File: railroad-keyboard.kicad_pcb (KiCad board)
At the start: 2 copper layers, 208 parts, among them SW1 SW_Push, U1 ATmega32U4-AU, Y1 16MHz

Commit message: Further PCB WIP
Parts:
- moved MX609 403.5 mm to (388.1, 304.8)
- moved MX509 403.0 mm to (407.2, 285.8)
- moved MX810 390.5 mm to (438.1, 328.6)
- moved MX909 377.9 mm to (419.1, 328.6)
- moved MX908 370.8 mm to (371.5, 323.9)
- moved MX809 365.2 mm to (400.1, 328.6)
- moved MX808 345.6 mm to (342.9, 323.9)
- moved MX906 326.7 mm to (288.1, 328.6)
- moved MX708 323.1 mm to (361.9, 304.8)
- moved MX907 314.9 mm to (314.3, 328.6)
- moved MX608 311.5 mm to (342.9, 304.8)
- moved MX600 303.1 mm to (9.53, 309.6)
- moved MX904 300.7 mm to (202.4, 328.6)
- moved MX707 298.6 mm to (323.9, 304.8)
- moved MX702 285.7 mm to (123.8, 304.8)
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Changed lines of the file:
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@@
   )
   (module MX_Alps_Hybrid:MX-1U-NoLED (layer F.Cu)
-    (at 195.78 23.78875)
+    (at 419.1 328.6125)
     (fp_text reference MX909 (at 0 3.175) (layer Dwgs.User)
       (effects (font (size 1 1) (thickness 0.15)))
@@
   )
   (module MX_Alps_Hybrid:MX-1.5U-NoLED (layer F.Cu)
-    (at 57.8425 126.06875)
+    (at 371.475 323.85)
     (fp_text reference MX908 (at 0 3.175) (layer Dwgs.User)
       (effects (font (size 1 1) (thickness 0.15)))
@@
   )
   (module MX_Alps_Hybrid:MX-1U-NoLED (layer F.Cu)
-    (at 43.56 167.74875)
+    (at 314.325 328.6125)
     (fp_text reference MX907 (at 0 3.175) (layer Dwgs.User)
       (effects (font (size 1 1) (thickness 0.15)))
@@
   )
   (module MX_Alps_Hybrid:MX-1.75U-NoLED (layer F.Cu)
-    (at 69.75375 85.66875)
+    (at 288.13125 328.6125)
     (fp_text reference MX906 (at 0 3.175) (layer Dwgs.User)
       (effects (font (size 1 1) (thickness 0.15)))
@@
   )
   (module MX_Alps_Hybrid:MX-2.25U-NoLED (layer F.Cu)
-    (at 504.825 284.95625)
+    (at 250.03125 328.6125)
     (fp_text reference MX905 (at 0 3.175) (layer Dwgs.User)
       (effects (font (size 1 1) (thickness 0.15)))
@@
   )
   (module MX_Alps_Hybrid:MX-2.75U-NoLED (layer F.Cu)
-    (at 494.50625 257.175)
+    (at 202.40625 328.6125)
     (fp_text reference MX904 (at 0 3.175) (layer Dwgs.User)
       (effects (font (size 1 1) (thickness 0.15)))
@@
   )
   (module MX_Alps_Hybrid:MX-1.75U-NoLED (layer F.Cu)
-    (at 25.74375 107.14875)
+    (at 159.54375 328.6125)
     (fp_text reference MX903 (at 0 3.175) (layer Dwgs.User)
       (effects (font (size 1 1) (thickness 0.15)))
@@
   )
   (module MX_Alps_Hybrid:MX-1U-NoLED (layer F.Cu)
-    (at 53.08 146.26875)
+    (at 133.35 328.6125)
     (fp_text reference MX902 (at 0 3.175) (layer Dwgs.User)
       (effects (font (size 1 1) (thickness 0.15)))
@@
   )
   (module MX_Alps_Hybrid:MX-1.25U-NoLED (layer F.Cu)
-    (at 89.95125 105.86875)
+    (at 83.34375 323.85)
     (fp_text reference MX901 (at 0 3.175) (layer Dwgs.User)
       (effects (font (size 1 1) (thickness 0.15)))
@@
   )
   (module MX_Alps_Hybrid:MX-1U-NoLED (layer F.Cu)
-    (at 82.8 126.06875)
+    (at 28.575 328.6125)
     (fp_text reference MX900 (at 0 3.175) (layer Dwgs.User)
       (effects (font (size 1 1) (thickness 0.15)))
@@
   )
   (module MX_Alps_Hybrid:MX-1U-NoLED (layer F.Cu)
-    (at 170.82 43.98875)
+    (at 438.15 328.6125)
     (fp_text reference MX810 (at 0 3.175) (layer Dwgs.User)
       (effects (font (size 1 1) (thickness 0.15)))
@@
   )
   (module MX_Alps_Hybrid:MX-1U-NoLED (layer F.Cu)
-    (at 112.53 103.43875)
+    (at 400.05 328.6125)
     (fp_text reference MX809 (at 0 3.175) (layer Dwgs.User)
       (effects (font (size 1 1) (thickness 0.15)))
@@
   )
   (module MX_Alps_Hybrid:MX-1.5U-NoLED (layer F.Cu)
-    (at 116.1425 63.03875)
+    (at 342.9 323.85)
     (fp_text reference MX808 (at 0 3.175) (layer Dwgs.User)
       (effects (font (size 1 1) (thickness 0.15)))
@@
   )
   (module MX_Alps_Hybrid:MX-1.25U-NoLED (layer F.Cu)
-    (at 20.98125 167.74875)
+    (at 107.15625 323.85)
     (fp_text reference MX802 (at 0 3.175) (layer Dwgs.User)
       (effects (font (size 1 1) (thickness 0.15)))
@@
   )
   (module MX_Alps_Hybrid:MX-1.5U-NoLED (layer F.Cu)
-    (at 62.6125 105.86875)
+    (at 57.15 323.85)
     (fp_text reference MX801 (at 0 3.175) (layer Dwgs.User)
       (effects (font (size 1 1) (thickness 0.15)))
@@
   )
   (module MX_Alps_Hybrid:MX-1U-NoLED (layer F.Cu)
-    (at 73.28 146.26875)
+    (at 9.525 328.6125)
     (fp_text reference MX800 (at 0 3.175) (layer Dwgs.User)
       (effects (font (size 1 1) (thickness 0.15)))
@@
   )
   (module MX_Alps_Hybrid:MX-1U-NoLED (layer F.Cu)
-    (at 224.2 124.78875)
+    (at 419.1 309.5625)
     (fp_text reference MX709 (at 0 3.175) (layer Dwgs.User)
       (effects (font (size 1 1) (thickness 0.15)))
@@
   )
   (module MX_Alps_Hybrid:MX-1U-NoLED (layer F.Cu)
-    (at 126.81 83.23875)
+    (at 361.95 304.8)
     (fp_text reference MX708 (at 0 3.175) (layer Dwgs.User)
       (effects (font (size 1 1) (thickness 0.15)))
@@
   )
   (module MX_Alps_Hybrid:MX-1U-NoLED (layer F.Cu)
-    (at 147.01 64.18875)
+    (at 323.85 304.8)
     (fp_text reference MX707 (at 0 3.175) (layer Dwgs.User)
       (effects (font (size 1 1) (thickness 0.15)))
@@
   )
   (module MX_Alps_Hybrid:MX-1U-NoLED (layer F.Cu)
-    (at 211.22 43.98875)
+    (at 285.75 304.8)
     (fp_text reference MX706 (at 0 3.175) (layer Dwgs.User)
       (effects (font (size 1 1) (thickness 0.15)))
@@
   )
   (module MX_Alps_Hybrid:MX-1U-NoLED (layer F.Cu)
-    (at 256.38 23.78875)
+    (at 242.8875 304.8)
     (fp_text reference MX705 (at 0 3.175) (layer Dwgs.User)
       (effects (font (size 1 1) (thickness 0.15)))
@@
   )
   (module MX_Alps_Hybrid:MX-1U-NoLED (layer F.Cu)
-    (at 133.88 144.98875)
+    (at 204.7875 304.8)
     (fp_text reference MX704 (at 0 3.175) (layer Dwgs.User)
       (effects (font (size 1 1) (thickness 0.15)))
@@
   )
   (module MX_Alps_Hybrid:MX-1U-NoLED (layer F.Cu)
-    (at 231.42 43.98875)
+    (at 161.925 304.8)
     (fp_text reference MX703 (at 0 3.175) (layer Dwgs.User)
       (effects (font (size 1 1) (thickness 0.15)))
@@
   )
   (module MX_Alps_Hybrid:MX-1U-NoLED (layer F.Cu)
-    (at 175.58 23.78875)
+    (at 123.825 304.8)
     (fp_text reference MX702 (at 0 3.175) (layer Dwgs.User)
       (effects (font (size 1 1) (thickness 0.15)))
@@
   )
   (module MX_Alps_Hybrid:MX-1U-NoLED (layer F.Cu)
-    (at 147.01 84.38875)
+    (at 85.725 304.8)
     (fp_text reference MX701 (at 0 3.175) (layer Dwgs.User)
       (effects (font (size 1 1) (thickness 0.15)))
@@
   )
   (module MX_Alps_Hybrid:MX-1.75U-NoLED (layer F.Cu)
-    (at 25.74375 127.34875)
+    (at 388.14375 304.8)
     (fp_text reference MX609 (at 0 3.175) (layer Dwgs.User)
       (effects (font (size 1 1) (thickness 0.15)))
@@
   )
   (module MX_Alps_Hybrid:MX-1U-NoLED (layer F.Cu)
-    (at 63.76 166.46875)
+    (at 342.9 304.8)
     (fp_text reference MX608 (at 0 3.175) (layer Dwgs.User)
       (effects (font (size 1 1) (thickness 0.15)))
@@
   )
   (module MX_Alps_Hybrid:MX-1U-NoLED (layer F.Cu)
-    (at 191.02 43.98875)
+    (at 304.8 304.8)
     (fp_text reference MX607 (at 0 3.175) (layer Dwgs.User)
       (effects (font (size 1 1) (thickness 0.15)))
@@
   )
   (module MX_Alps_Hybrid:MX-1U-NoLED (layer F.Cu)
-    (at 93.48 146.26875)
+    (at 266.7 304.8)
     (fp_text reference MX606 (at 0 3.175) (layer Dwgs.User)
       (effects (font (size 1 1) (thickness 0.15)))
@@
   )
   (module MX_Alps_Hybrid:MX-1U-NoLED (layer F.Cu)
-    (at 215.98 23.78875)
+    (at 223.8375 304.8)
     (fp_text reference MX605 (at 0 3.175) (layer Dwgs.User)
       (effects (font (size 1 1) (thickness 0.15)))
@@
   )
   (module MX_Alps_Hybrid:MX-1U-NoLED (layer F.Cu)
-    (at 187.41 84.38875)
+    (at 180.975 304.8)
     (fp_text reference MX604 (at 0 3.175) (layer Dwgs.User)
       (effects (font (size 1 1) (thickness 0.15)))
@@
   )
   (module MX_Alps_Hybrid:MX-1U-NoLED (layer F.Cu)
-    (at 167.21 84.38875)
+    (at 142.875 304.8)
     (fp_text reference MX603 (at 0 3.175) (layer Dwgs.User)
       (effects (font (size 1 1) (thickness 0.15)))
@@
   )
   (module MX_Alps_Hybrid:MX-1U-NoLED (layer F.Cu)
-    (at 83.96 166.46875)
+    (at 104.775 304.8)
     (fp_text reference MX602 (at 0 3.175) (layer Dwgs.User)
       (effects (font (size 1 1) (thickness 0.15)))
@@
   )
   (module MX_Alps_Hybrid:MX-2.75U-NoLED (layer F.Cu)
-    (at 35.26875 44.62875)
+    (at 50.00625 304.8)
     (fp_text reference MX601 (at 0 3.175) (layer Dwgs.User)
       (effects (font (size 1 1) (thickness 0.15)))
@@
   )
   (module MX_Alps_Hybrid:MX-1U-NoLED (layer F.Cu)
-    (at 187.41 64.18875)
+    (at 9.525 309.5625)
     (fp_text reference MX600 (at 0 3.175) (layer Dwgs.User)
       (effects (font (size 1 1) (thickness 0.15)))
@@
   )
   (module MX_Alps_Hybrid:MX-1.75U-NoLED (layer F.Cu)
-    (at 69.75375 65.46875)
+    (at 407.19375 285.75)
     (fp_text reference MX509 (at 0 3.175) (layer Dwgs.User)
       (effects (font (size 1 1) (thickness 0.15)))
@@
   )
   (module MX_Alps_Hybrid:MX-1U-NoLED (layer F.Cu)
-    (at 143.4 104.58875)
+    (at 361.95 285.75)
     (fp_text reference MX508 (at 0 3.175) (layer Dwgs.User)
       (effects (font (size 1 1) (thickness 0.15)))
@@
   )
   (module MX_Alps_Hybrid:MX-1U-NoLED (layer F.Cu)
-    (at 167.21 64.18875)
+    (at 323.85 285.75)
     (fp_text reference MX507 (at 0 3.175) (layer Dwgs.User)
       (effects (font (size 1 1) (thickness 0.15)))
@@
   )
   (module MX_Alps_Hybrid:MX-1U-NoLED (layer F.Cu)
-    (at 207.61 84.38875)
+    (at 381 285.75)
     (fp_text reference MX409 (at 0 3.175) (layer Dwgs.User)
       (effects (font (size 1 1) (thickness 0.15)))
@@
   )
   (module MX_Alps_Hybrid:MX-1U-NoLED (layer F.Cu)
-    (at 227.81 64.18875)
+    (at 342.9 285.75)
     (fp_text reference MX408 (at 0 3.175) (layer Dwgs.User)
       (effects (font (size 1 1) (thickness 0.15)))
@@
   )
   (module MX_Alps_Hybrid:MX-1U-NoLED (layer F.Cu)
-    (at 251.62 43.98875)
+    (at 304.8 285.75)
     (fp_text reference MX407 (at 0 3.175) (layer Dwgs.User)
       (effects (font (size 1 1) (thickness 0.15)))

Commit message: Diodes placed
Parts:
- D0, D1, D10, D100, D101, D102, D103, D104, D105, D106, D107, D108, D109, D2, D200, D201, D202, D203, D204, D205, D206, D207, D208, D209, D3, D300, D301, D302, D303, D304, D305, D306, D307, D308, D309, D4, D400, D401, D402, D403, D404, D405, D406, D407, D408, D409, D410, D5, D501, D502, D503, D504, D505, D506, D507, D508, D509, D6, D600, D601, D602, D603, D604, D605, D606, D607, D608, D609, D7, D701, D702, D703, D704, D705, D706, D707, D708, D709, D8, D800, D801, D802, D808, D809, D810, D9, D900, D901, D902, D903, D904, D905, D906, D907, D908, D909: moved to B.Cu
- moved D810 435.1 mm to (446.4, 331.2), turned to 90 degrees
- moved D909 420.2 mm to (427.2, 331.1), turned to 90 degrees
- moved D709 408.7 mm to (427.2, 312.2), turned to 90 degrees
- moved D410 378.5 mm to (436.1, 284.5)
- moved D609 367.0 mm to (396.4, 307.3), turned to 90 degrees
- moved D509 364.4 mm to (415.4, 288.3), turned to 90 degrees
- moved D809 364.0 mm to (408.2, 331.1), turned to 90 degrees
- moved D708 349.9 mm to (370.1, 307.3), turned to 90 degrees
- moved D908 347.9 mm to (379.6, 326.4), turned to 90 degrees
- moved D10 345.0 mm to (446.3, 250.2), turned to 90 degrees
- moved D309 344.8 mm to (417.7, 269.2), turned to 90 degrees
- moved D109 332.5 mm to (427.2, 250.2), turned to 90 degrees
- moved D409 329.3 mm to (389.1, 288.3), turned to 90 degrees
- moved D907 328.0 mm to (322.5, 331.1), turned to 270 degrees
- moved D209 327.4 mm to (394.0, 269.2), turned to 90 degrees
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
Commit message: Completion of first draft
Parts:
- C1, C2, C3, C4, C5, C6, C7, F1, R1, R2, R3, R4, SW1, U1, USB1, Y1: moved to B.Cu
- MX0, MX1, MX10, MX101, MX102, MX103, MX104, MX105, MX106, MX107, MX108, MX109, MX2, MX200, MX202, MX203, MX204, MX205, MX206, MX207, MX208, MX3, MX301, MX302, MX303, MX304, MX305, MX306, MX307, MX308, MX309, MX4, MX402, MX403, MX404, MX405, MX406, MX407, MX408, MX409, MX5, MX501, MX502, MX503, MX504, MX505, MX506, MX507, MX6, MX600, MX602, MX603, MX604, MX605, MX606, MX607, MX608, MX7, MX701, MX702, MX703, MX704, MX705, MX706, MX707, MX708, MX709, MX8, MX800, MX809, MX810, MX900, MX902, MX907, MX909: footprint MX_Alps_Hybrid:MX-1U-NoLED -> MX_Only:MXOnly-1U-NoLED
- MX100, MX9: footprint MX_Alps_Hybrid:MX-2U-NoLED -> MX_Only:MXOnly-2U-NoLED
- MX201, MX209, MX300, MX801, MX808, MX908: footprint MX_Alps_Hybrid:MX-1.5U-NoLED -> MX_Only:MXOnly-1.5U-NoLED
- MX400, MX802, MX901: footprint MX_Alps_Hybrid:MX-1.25U-NoLED -> MX_Only:MXOnly-1.25U-NoLED
- MX401, MX905: footprint MX_Alps_Hybrid:MX-2.25U-NoLED -> MX_Only:MXOnly-2.25U-NoLED
- MX410: footprint MX_Alps_Hybrid:MX-ISO -> MX_Only:MXOnly-ISO-ROTATED-ReversedStabilizers-NoLED
- MX508: footprint MX_Alps_Hybrid:MX-1U-NoLED -> MX_Only:MXOnly-1.75U-NoLED
- MX509, MX609, MX903, MX906: footprint MX_Alps_Hybrid:MX-1.75U-NoLED -> MX_Only:MXOnly-1.75U-NoLED
- MX601, MX904: footprint MX_Alps_Hybrid:MX-2.75U-NoLED -> MX_Only:MXOnly-2.75U-NoLED
- moved R4 442.0 mm to (445.5, 315.9), turned to 90 degrees
- moved R1 441.6 mm to (434.2, 298.3), turned to 180 degrees
- moved U1 440.2 mm to (438.8, 306.7)
- moved R2 415.3 mm to (431.5, 250.8)
- moved R3 415.2 mm to (428.2, 248.9)
- moved C1 395.2 mm to (440.6, 292.7), turned to 90 degrees
- moved USB1 382.9 mm to (428.6, 241.8), turned to 270 degrees
- moved C6 341.0 mm to (441.1, 316.1), turned to 180 degrees
- moved C3 331.4 mm to (428.6, 306.6), turned to 270 degrees
- moved C5 327.3 mm to (430.0, 314.2), turned to 270 degrees
- moved C2 325.2 mm to (432.1, 291.3), turned to 90 degrees
- moved C7 314.8 mm to (440.3, 258.6), turned to 180 degrees
- moved Y1 314.1 mm to (436.4, 292.4), turned to 180 degrees
- moved C4 307.5 mm to (433.8, 258.6)
- moved F1 286.5 mm to (422.1, 241.3), turned to 90 degrees
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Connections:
- U1 pad 10: ROW2 -> COL2
- U1 pad 11: ROW3 -> COL3
- U1 pad 12: ROW7 -> COL4
- U1 pad 18: COL0 -> COL5
- U1 pad 19: COL1 -> COL6
- U1 pad 20: COL2 -> COL7
- U1 pad 21: COL3 -> COL8
- U1 pad 22: COL5 -> COL9
- U1 pad 25: COL4 -> COL10
- U1 pad 26: COL6 -> ROW0
- U1 pad 27: COL7 -> ROW1
- U1 pad 28: ROW4 -> ROW2
- U1 pad 29: ROW5 -> ROW3
- U1 pad 30: ROW6 -> ROW5
- U1 pad 31: ROW8 -> ROW4
- U1 pad 32: ROW9 -> ROW8
- U1 pad 39: COL10 -> ROW9
- U1 pad 40: COL9 -> ROW6
- U1 pad 41: COL8 -> ROW7
- U1 pad 8: ROW0 -> COL0
- U1 pad 9: ROW1 -> COL1
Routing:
- net COL0: track 0.00 -> 670.5 mm, vias 0 -> 2
- net COL1: track 0.00 -> 603.5 mm, vias 0 -> 2
- net GND: track 0.00 -> 570.5 mm, vias 0 -> 5
- net COL2: track 0.00 -> 527.9 mm, vias 0 -> 2
- net ROW0: track 0.00 -> 495.6 mm, vias 0 -> 2
- net Net-(R1-Pad2): track 0.00 -> 475.9 mm, vias 0 -> 2
- net ROW2: track 0.00 -> 475.2 mm, vias 0 -> 2
- net ROW8: track 0.00 -> 464.9 mm, vias 0 -> 2
- net ROW4: track 0.00 -> 461.1 mm, vias 0 -> 2
- net ROW1: track 0.00 -> 457.7 mm, vias 0 -> 2
- net ROW3: track 0.00 -> 450.7 mm, vias 0 -> 2
- net COL3: track 0.00 -> 446.2 mm, vias 0 -> 2
- net COL4: track 0.00 -> 442.0 mm, vias 0 -> 3
- net ROW6: track 0.00 -> 435.5 mm
- net ROW9: track 0.00 -> 428.8 mm
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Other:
- net class Default: trace_width 0.25 -> 0.254
- net class Net Power added: clearance 0.2, trace_width 0.381, via_dia 0.8, via_drill 0.4

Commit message: Further major revisions
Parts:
- removed USB1: Molex-0548190589, random-keyboard-parts:Molex-0548190589
- added C8: 4.7uF, Capacitor_SMD:C_0805_2012Metric, B.Cu at (187.4, 250.4)
- added J1: 1734510-1, usb-mini-1734510-1:TE_1734510-1, B.Cu at (192.5, 239.9)
- added R5: 1m, Resistor_SMD:R_0805_2012Metric, B.Cu at (187.4, 247.3)
- added R6: 10k, Resistor_SMD:R_0805_2012Metric, F.Cu at (193.0, 286.3)
- added R7: 4.7k, Resistor_SMD:R_0805_2012Metric, B.Cu at (433.5, 241.3)
- added R8: 4.7k, Resistor_SMD:R_0805_2012Metric, B.Cu at (433.6, 244.1)
- added U2: TRRS, Keebio-Parts:TRRS-PJ-320A, B.Cu at (428.6, 238.1)
- C1, C2, C3, C5, C7: footprint Diode_SMD:D_SOD-123 -> Capacitor_SMD:C_0805_2012Metric
- C4: value 10uF -> 4.7uF; footprint Diode_SMD:D_SOD-123 -> Capacitor_SMD:C_0805_2012Metric
- C6: footprint Diode_SMD:D_SOD-123 -> Capacitor_SMD:C_0805_2012Metric; moved to F.Cu
- MX508: footprint MX_Only:MXOnly-1.75U-NoLED -> MX_Only:MXOnly-1U-NoLED
- R1, R2, R3: moved to F.Cu
- moved D709 254.4 mm to (176.3, 355.0)
- moved C5 254.4 mm to (178.9, 355.0)
- moved C6 250.0 mm to (194.3, 276.1), turned to 90 degrees
- moved C1 249.7 mm to (192.8, 261.1), turned to 180 degrees
- moved C3 248.8 mm to (181.6, 276.5)
- moved U1 247.9 mm to (192.8, 276.2)
- moved R4 247.2 mm to (200.7, 282.0)
- moved Y1 245.1 mm to (192.9, 264.8)
- moved C2 244.3 mm to (189.2, 264.9), turned to 270 degrees
- moved R1 243.7 mm to (191.5, 276.1), turned to 90 degrees
- moved C7 241.8 mm to (198.6, 251.5), turned to 90 degrees
- moved R2 237.6 mm to (193.9, 253.0), turned to 90 degrees
- moved C4 237.3 mm to (196.6, 251.5), turned to 90 degrees
- moved R3 236.3 mm to (191.9, 253.0), turned to 90 degrees
- moved F1 229.3 mm to (192.9, 247.8), turned to 180 degrees
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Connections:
- U1 pad 18: COL5 -> LHD0
- U1 pad 19: COL6 -> LHD1
- U1 pad 20: COL7 -> ROW0
- U1 pad 21: COL8 -> ROW1
- U1 pad 22: COL9 -> ROW2
- U1 pad 25: COL10 -> COL5
- U1 pad 26: ROW0 -> COL6
- U1 pad 27: ROW1 -> COL7
- U1 pad 28: ROW2 -> COL8
- U1 pad 29: ROW3 -> COL9
- U1 pad 30: ROW5 -> COL10
- U1 pad 31: ROW4 -> ROW3
- U1 pad 32: ROW8 -> ROW4
- U1 pad 37: Net-(U1-Pad37) -> ROW5
- U1 pad 38: Net-(U1-Pad38) -> ROW6
- U1 pad 39: ROW9 -> ROW7
- U1 pad 40: ROW6 -> ROW8
- U1 pad 41: ROW7 -> ROW9
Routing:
- net COL0: track 670.5 -> 0.00 mm, vias 2 -> 0
- net COL1: track 603.5 -> 0.00 mm, vias 2 -> 0
- net COL2: track 527.9 -> 0.00 mm, vias 2 -> 0
- net ROW8: track 464.9 -> 0.00 mm, vias 2 -> 0
- net ROW4: track 461.1 -> 0.00 mm, vias 2 -> 0
- net ROW6: track 435.5 -> 0.00 mm
- net ROW9: track 428.8 -> 0.00 mm
- net ROW5: track 378.8 -> 0.00 mm, vias 2 -> 0
- net COL5: track 372.5 -> 0.00 mm, vias 2 -> 0
- net COL6: track 363.2 -> 0.00 mm, vias 1 -> 0
- net ROW7: track 356.0 -> 0.00 mm
- net COL7: track 295.1 -> 0.00 mm, vias 2 -> 0
- net COL4: track 442.0 -> 168.1 mm, vias 3 -> 0
- net COL8: track 266.9 -> 0.00 mm, vias 2 -> 0
- net LHD1: track 0.00 -> 266.4 mm, vias 0 -> 2
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
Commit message: Second tracing draft
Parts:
- C6, R1, R2, R3, R6: moved to B.Cu
- moved D709 248.7 mm to (421.6, 314.2)
- moved C5 72.5 mm to (184.9, 282.8)
- moved C6 17.4 mm to (176.9, 276.5)
- moved R1 14.1 mm to (178.4, 281.2)
- moved R6 8.13 mm to (184.9, 286.4)
- moved R2 2.16 mm to (194.1, 250.9)
- moved R3 1.25 mm to (191.4, 251.9)
- moved D604 0.25 mm to (183.5, 309.5)
- turned C8 to 0 degrees
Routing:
- net ROW8: track 0.00 -> 481.4 mm, vias 0 -> 2
- net ROW4: track 0.00 -> 463.8 mm
- net ROW9: track 0.00 -> 457.2 mm, vias 0 -> 2
- net ROW6: track 0.00 -> 416.9 mm, vias 0 -> 2
- net COL9: track 0.00 -> 375.4 mm, vias 0 -> 1
- net ROW7: track 0.00 -> 371.5 mm, vias 0 -> 2
- net ROW5: track 0.00 -> 349.1 mm, vias 0 -> 2
- net COL0: track 0.00 -> 345.1 mm, vias 0 -> 1
- net COL10: track 0.00 -> 326.9 mm
- net COL8: track 0.00 -> 316.0 mm, vias 0 -> 1
- net COL1: track 0.00 -> 295.3 mm, vias 0 -> 1
- net COL7: track 0.00 -> 263.8 mm, vias 0 -> 1
- net COL2: track 0.00 -> 248.9 mm, vias 0 -> 1
- net COL6: track 0.00 -> 222.7 mm, vias 0 -> 1
- net COL5: track 0.00 -> 182.6 mm, vias 0 -> 1
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
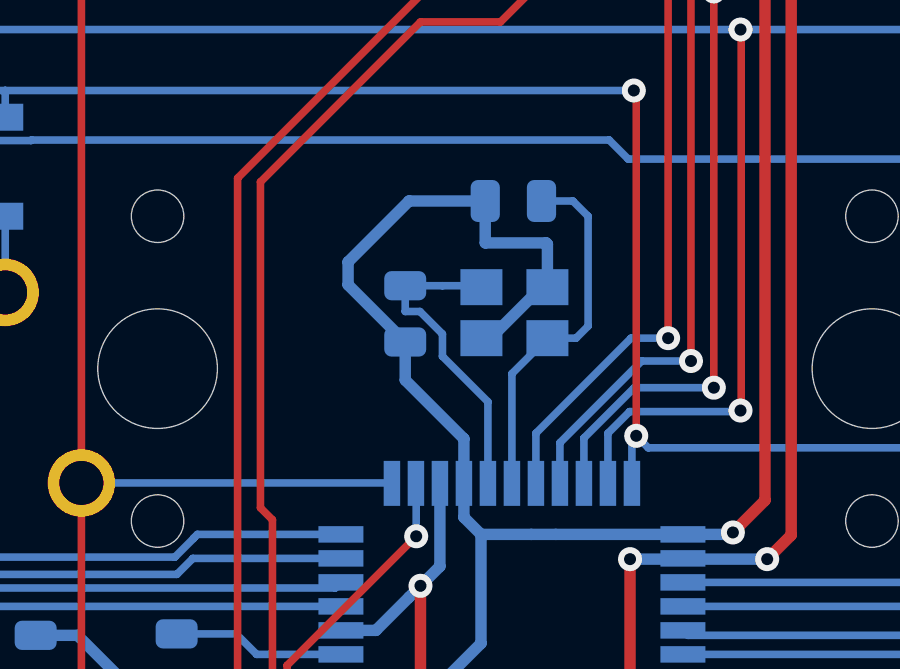
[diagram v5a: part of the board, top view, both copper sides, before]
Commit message: Adjustments to crystal placement
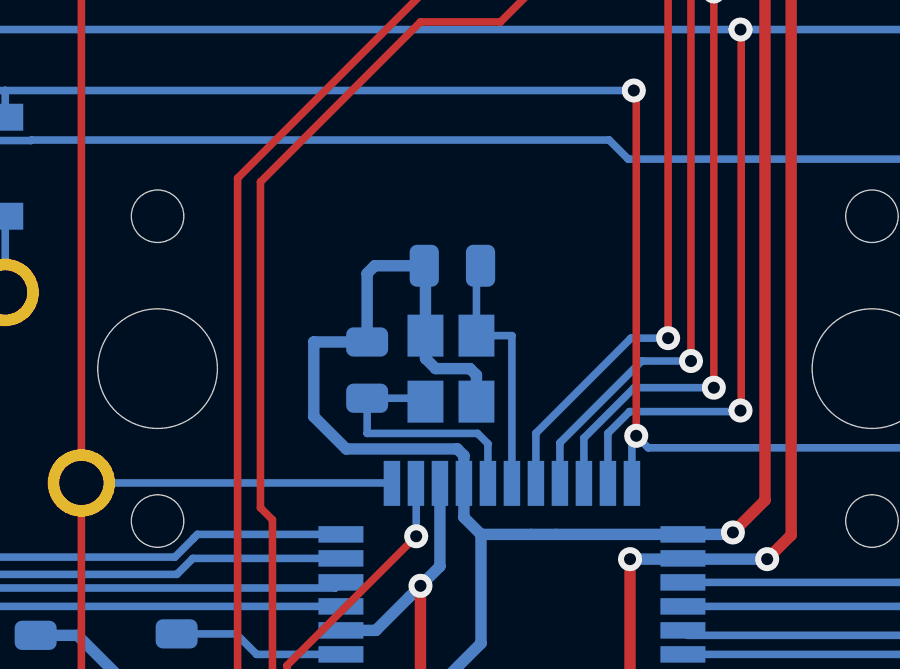
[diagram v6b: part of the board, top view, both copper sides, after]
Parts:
- moved C1 2.96 mm to (190.8, 263.3)
- moved Y1 2.82 mm to (190.8, 266.7), turned to 270 degrees
- moved C2 2.26 mm to (188.0, 266.7), turned to 90 degrees
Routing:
- net Net-(C1-Pad1): track 12.3 -> 8.30 mm
- net Net-(C2-Pad1): track 10.6 -> 8.72 mm
- net GND: track 569.8 -> 568.4 mm

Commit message: Add ground fill
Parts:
- moved J1 2.41 mm to (192.5, 237.5)
- moved U2 2.38 mm to (428.6, 235.7)
- moved SW1 2.29 mm to (19.1, 238.4)
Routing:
- net GND: track 568.4 -> 266.3 mm, vias 2 -> 0
- net +5V: track 353.2 -> 350.6 mm
- net Net-(C8-Pad2): track 18.1 -> 20.5 mm
- net VCC: track 3.15 -> 5.48 mm
- net Net-(R1-Pad2): track 222.8 -> 225.1 mm
- net ROW0: track 453.7 -> 451.6 mm
- net D-: track 9.80 -> 11.5 mm
- net D+: track 6.43 -> 8.03 mm
- net ROW4: track 463.8 -> 462.7 mm
- net ROW5: track 349.1 -> 348.1 mm
- added copper zone on B.Cu, net GND
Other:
- board outline added: 452.4 x 104.8 mm
- board text added: "Railroad PCB W. Alex Ronke (NoPunIn10Did) Prototype 2020-07"
